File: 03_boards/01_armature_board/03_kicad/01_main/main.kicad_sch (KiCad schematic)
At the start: 61 parts, among them SW1 SW_Push, SW2 SW_Push, U1 STM32G431K8Tx, U2 LD1117S33, U3 MAX3485, U4 ADXL343, U5 74HC4051, Y1 ECS-80-20-18-TR

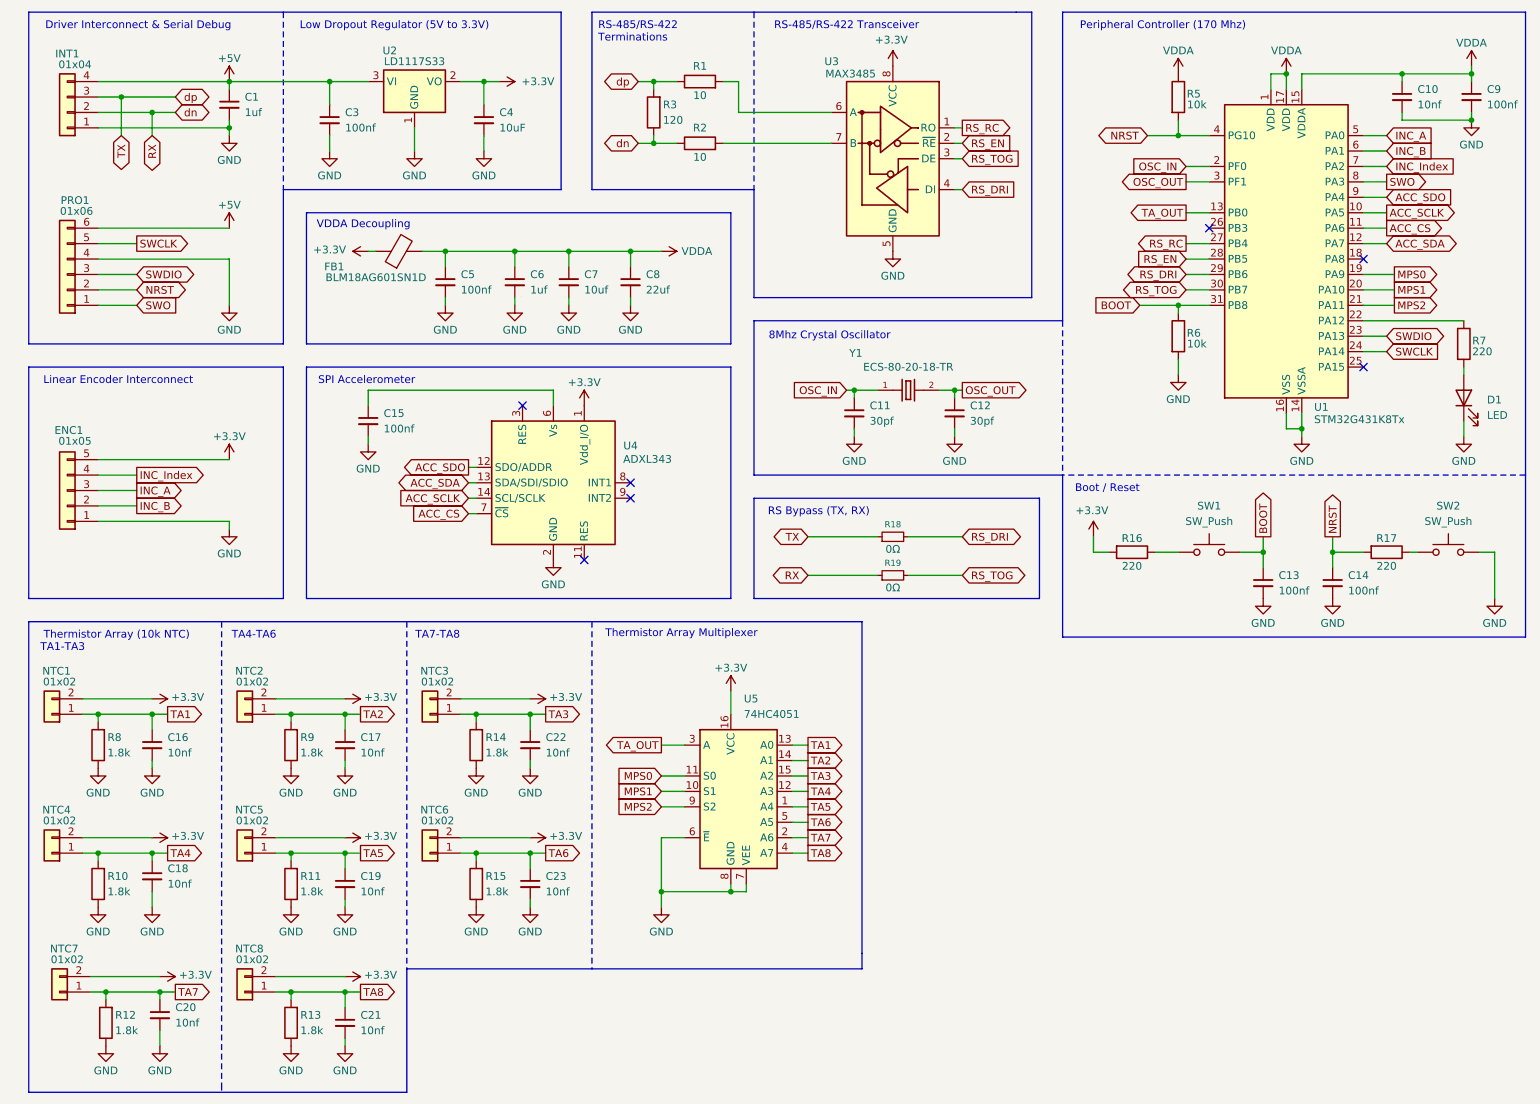
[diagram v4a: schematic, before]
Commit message: Updates to schematic and nearly finished first schematic draft
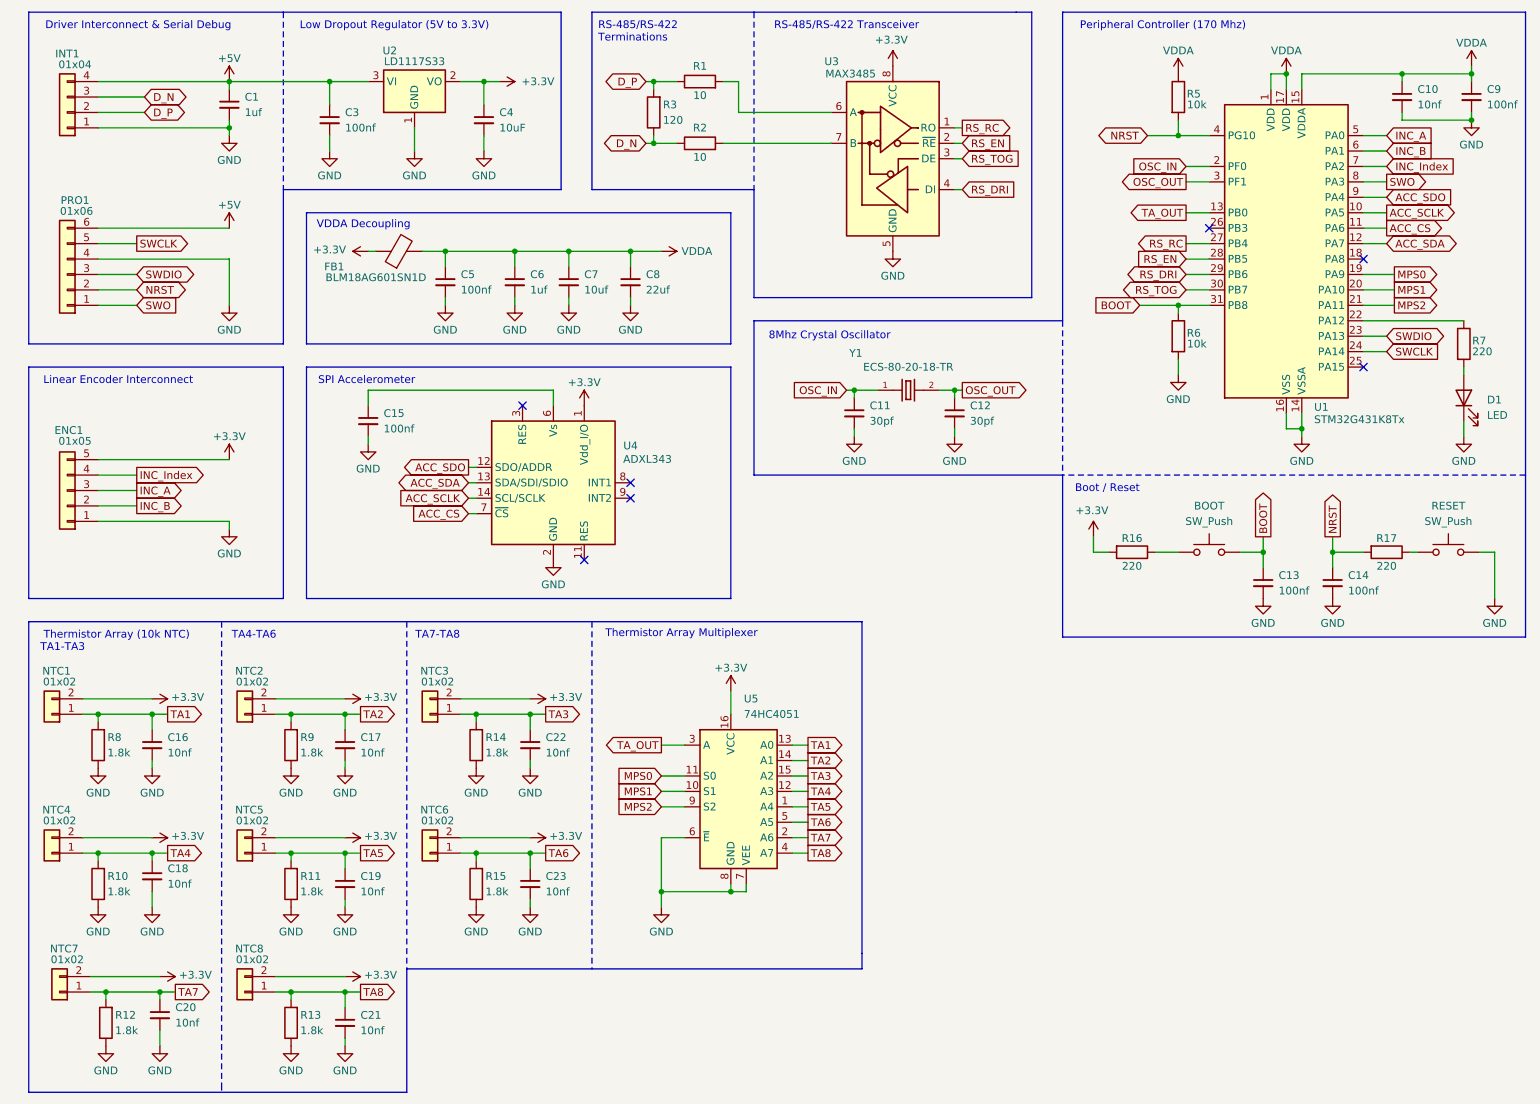
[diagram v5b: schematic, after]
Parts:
- removed R18, R19: 0Ω, Resistor_SMD:R_0603_1608Metric, symbol Device:R_Small
- renumbered SW1 to BOOT, SW2 to RESET
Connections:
- net RX renamed D_N
- net D_N: now also INT1.3 (Pin_3); no longer INT1.2 (Pin_2)
- net TX renamed D_P
- net D_P: now also INT1.2 (Pin_2); no longer INT1.3 (Pin_3)
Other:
- note removed: "RS Bypass (TX, RX)"

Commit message: Finished armature board development. Moving back to encoder board for images etc
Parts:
- D1: footprint LED_SMD:LED_1206_3216Metric -> LED_SMD:LED_0603_1608Metric_Pad1.05x0.95mm_HandSolder
- renumbered BOOT to BOOT1, RESET to RESET1
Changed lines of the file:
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@@
 		(dnp no)
 		(fields_autoplaced yes)
-		(property "Reference" "RESET"
+		(property "Reference" "RESET1"
 			(at 250.19 97.79 0)
 			(show_name no)
@@
 			(project "main"
 				(path "/d7317114-a4fd-40b5-9eea-fb013c7aed3d"
-					(reference "RESET")
+					(reference "RESET1")
 					(unit 1)
 				)
@@
 		(dnp no)
 		(fields_autoplaced yes)
-		(property "Reference" "BOOT"
+		(property "Reference" "BOOT1"
 			(at 210.82 97.79 0)
 			(show_name no)
@@
 			(project "main"
 				(path "/d7317114-a4fd-40b5-9eea-fb013c7aed3d"
-					(reference "BOOT")
+					(reference "BOOT1")
 					(unit 1)
 				)
@@
 			)
 		)
-		(property "Footprint" "LED_SMD:LED_1206_3216Metric"
+		(property "Footprint" "LED_SMD:LED_0603_1608Metric_Pad1.05x0.95mm_HandSolder"
 			(at 252.73 80.01 0)
 			(hide yes)

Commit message: Week 0xB | TeensySFOC & began work on hybrid model. (#44)
* Initial work on TeensySFOC board

* Added SFOC readme

* Schematic and referencing in the readme

* TeensySFOC & Armature REV 1

* Updated readme

* Few changes.

* Updated sub-readme

* Breakout not integration

* Added note.

* Update README.md

* Update README.md

* Deleted concenptual design

* Removed old driver pcb images from readme

* Update README.md

* Initial work on hybird model.

* Added a citation at the bottom of the repo

* Updated common point readme

* Fixed formatting

* Removed old implementation images & BOM

* Removed space.

* Moved link downwards

* Changed status.

* Updating formatting

* Formatting fix

* Removed images of board

* Update readme.md

* Renaming files & fixing formatting

* Updating hybrid model stuff

* Fixing formatting

* Formatting updates.

* Fixing formatting
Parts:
- ENC1: footprint Connector_JST:JST_PH_B5B-PH-K_1x05_P2.00mm_Vertical -> Connector_JST:JST_XH_B5B-XH-A_1x05_P2.50mm_Vertical
- INT1: footprint Connector_JST:JST_PH_B4B-PH-K_1x04_P2.00mm_Vertical -> Connector_JST:JST_XH_B4B-XH-A_1x04_P2.50mm_Vertical
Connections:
- net SWO: now also U1.26 (PB3); no longer U1.8 (PA3)
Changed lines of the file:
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@@
 	(title_block
 		(title "Armature Board")
-		(date "2026-07-22")
+		(date "2026-09-17")
+		(rev "1")
 	)
 	(text "Peripheral Controller (170 Mhz)"
@@
 	)
 	(no_connect
-		(at 210.82 52.07)
+		(at 236.22 44.45)
 	)
 	(no_connect
@@
 	(wire
 		(pts
-			(xy 236.22 44.45) (xy 240.03 44.45)
-		)
-		(stroke
-			(width 0)
-			(type default)
-		)
-	)
-	(wire
-		(pts
 			(xy 27.94 90.17) (xy 49.53 90.17)
 		)
@@
 	(wire
 		(pts
+			(xy 207.01 52.07) (xy 210.82 52.07)
+		)
+		(stroke
+			(width 0)
+			(type default)
+		)
+	)
+	(wire
+		(pts
 			(xy 120.65 161.29) (xy 120.65 163.83)
 		)
@@
 	(global_label "SWO"
 		(shape output)
-		(at 240.03 44.45 0)
+		(at 207.01 52.07 180)
 		(fields_autoplaced yes)
 		(effects
@@
 				(size 1.27 1.27)
 			)
-			(justify left)
+			(justify right)
 		)
 		(property "Intersheetrefs" "${INTERSHEET_REFS}"
-			(at 247.0066 44.45 0)
+			(at 200.0334 52.07 0)
 			(hide yes)
 			(show_name no)
@@
 					(size 1.27 1.27)
 				)
-				(justify left)
+				(justify right)
 			)
 		)
@@
 			)
 		)
-		(property "Footprint" "Connector_JST:JST_PH_B4B-PH-K_1x04_P2.00mm_Vertical"
+		(property "Footprint" "Connector_JST:JST_XH_B4B-XH-A_1x04_P2.50mm_Vertical"
 			(at 22.86 33.02 0)
 			(hide yes)
@@
 			)
 		)
-		(property "Footprint" "Connector_JST:JST_PH_B5B-PH-K_1x05_P2.00mm_Vertical"
+		(property "Footprint" "Connector_JST:JST_XH_B5B-XH-A_1x05_P2.50mm_Vertical"
 			(at 22.86 95.25 0)
 			(hide yes)
